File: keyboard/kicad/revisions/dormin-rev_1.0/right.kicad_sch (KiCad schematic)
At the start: 70 parts, among them SW1 SW_PUSH-MX_CHOC, SW10 SW_PUSH-MX_CHOC, SW11 SW_PUSH-MX_CHOC, SW12 SW_PUSH-MX_CHOC, SW13 SW_PUSH-MX_CHOC, SW14 SW_PUSH-MX_CHOC, SW15 SW_PUSH-MX_CHOC, SW16 SW_PUSH-MX_CHOC, SW17 SW_PUSH-MX_CHOC, SW19 SW_PUSH-MX_CHOC, SW2 SW_PUSH-MX_CHOC, SW20 SW_PUSH-MX_CHOC, SW21 SW_PUSH-MX_CHOC, SW22 SW_PUSH-MX_CHOC, SW3 SW_PUSH-MX_CHOC, SW4 SW_PUSH-MX_CHOC, SW5 SW_PUSH-MX_CHOC, SW6 SW_PUSH-MX_CHOC, SW7 SW_PUSH-MX_CHOC, SW8 SW_PUSH-MX_CHOC, SW9 SW_PUSH-MX_CHOC, U1 Seeeduino Xiao nRF52840

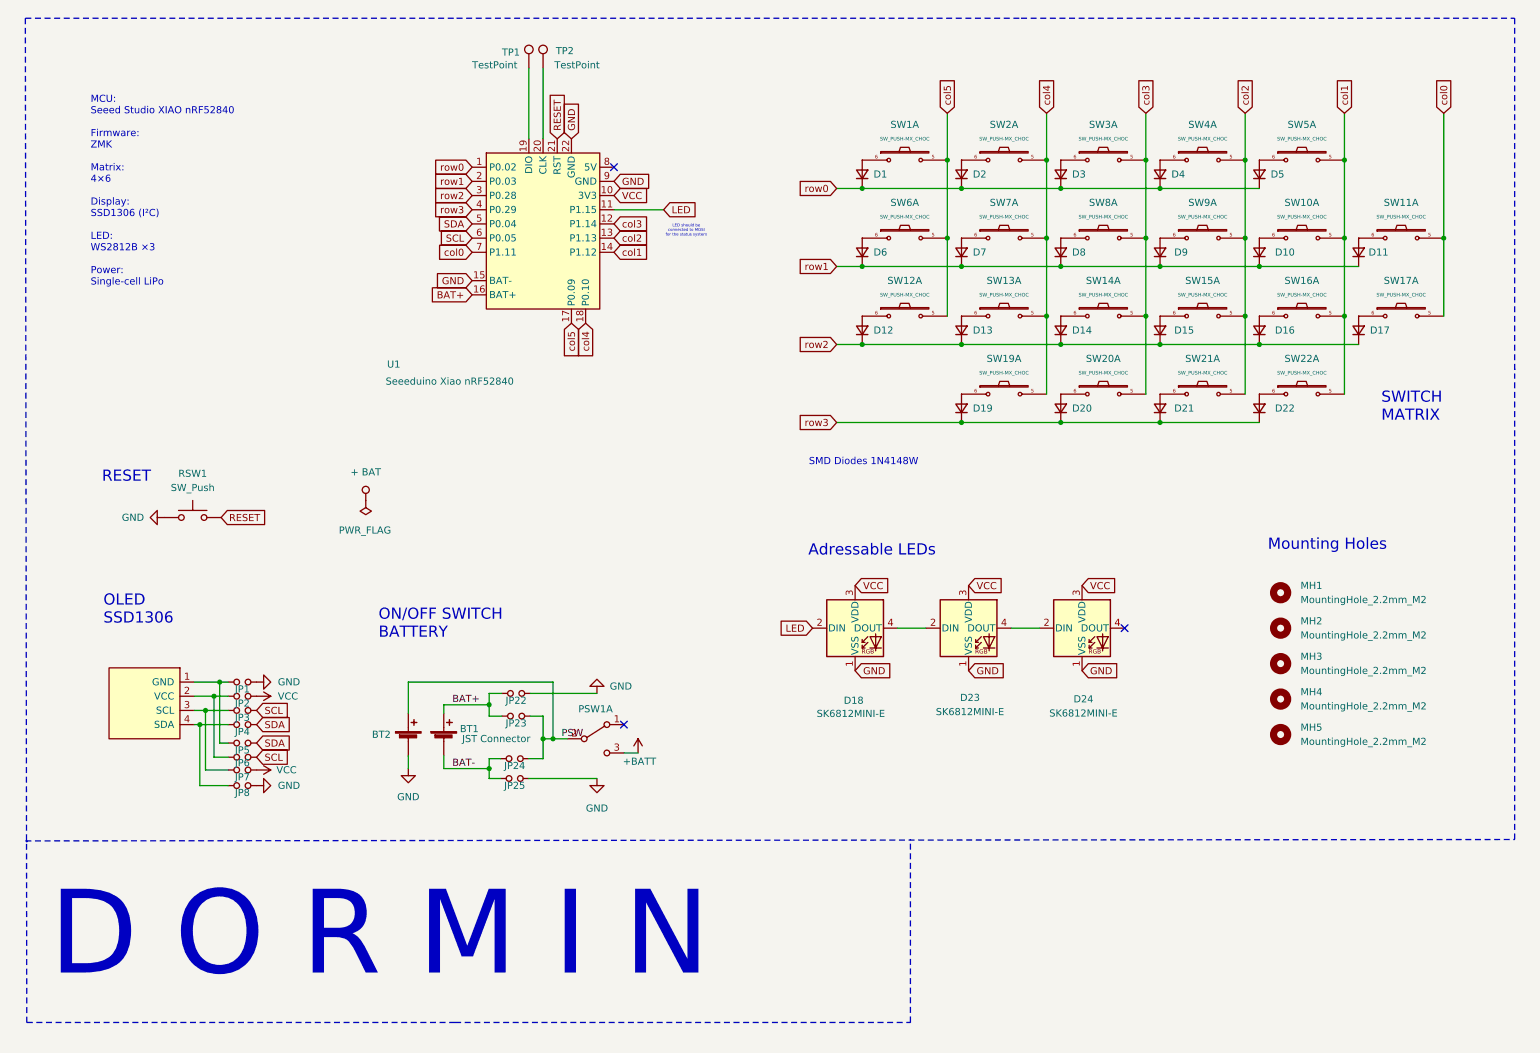
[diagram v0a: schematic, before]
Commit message: feat: update ergogen and kicad
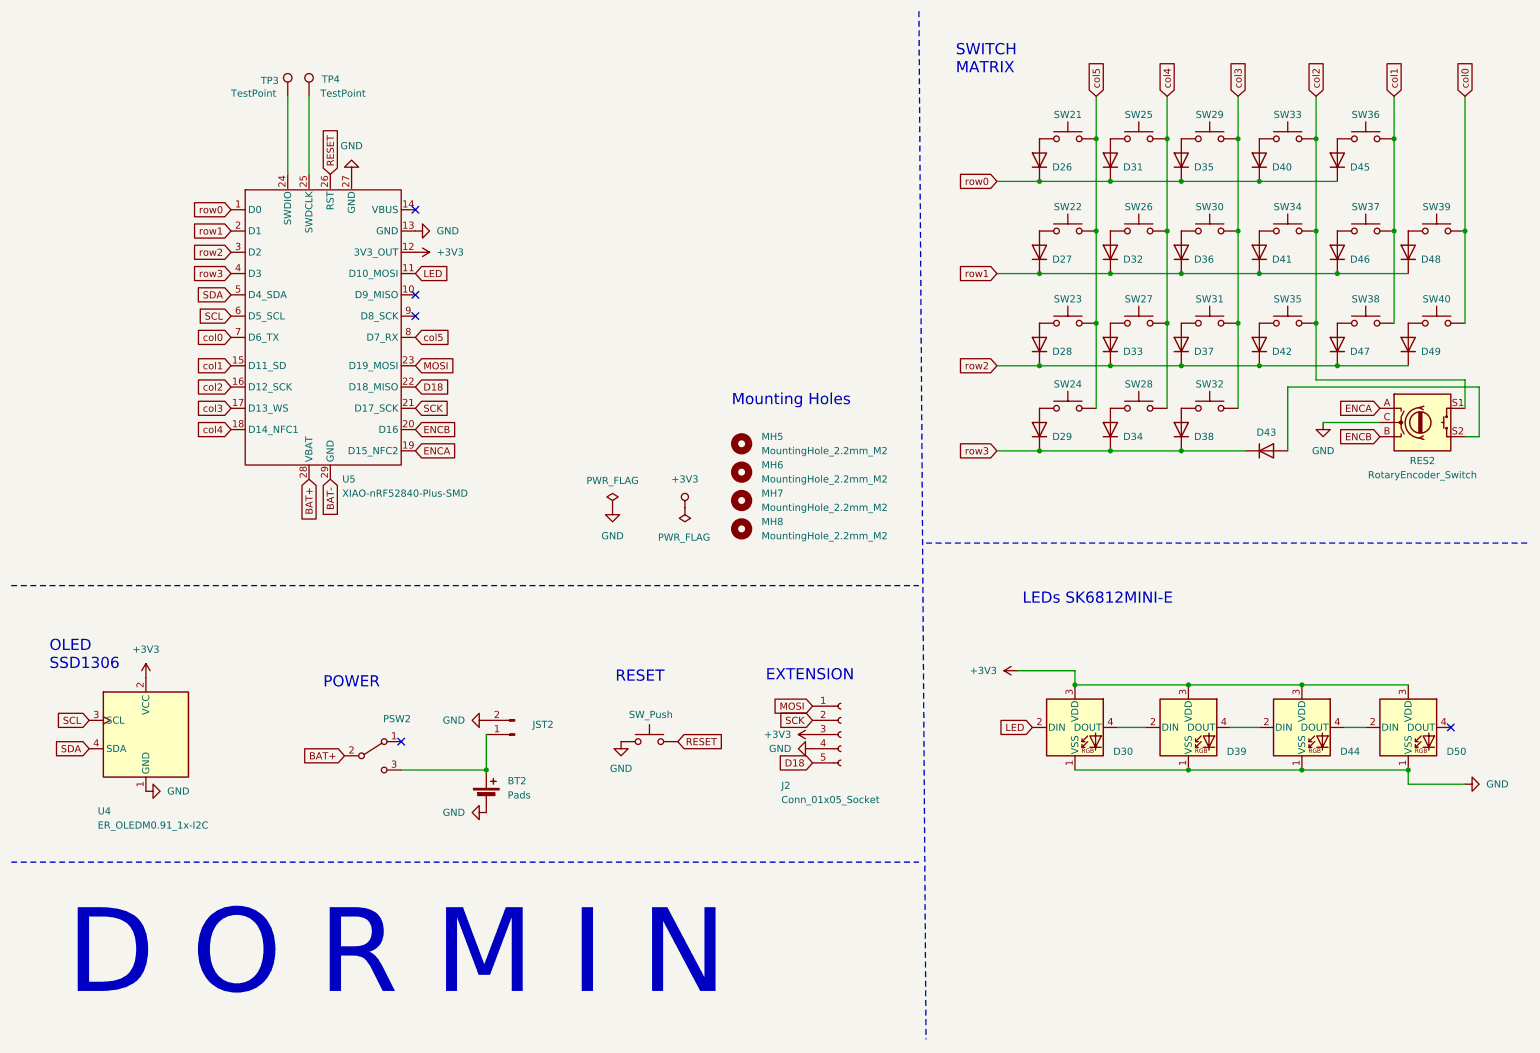
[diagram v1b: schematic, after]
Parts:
- removed BT1: JST Connector, KLOR:JST_PH_reversible, symbol Device:Battery_Cell
- removed D1, D10, D11, D12, D13, D14, D15, D16, D17, D19, D2, D20, D21, D22, D3, D4, D5, D6, D7, D8, D9: D_Small, KLOR:Diode_SOD123, symbol Device:D_Small
- removed D18, D23, D24: SK6812MINI-E, LED_SMD:LED_SK6812MINI-E_3.2x2.8mm_P1.5mm_ReverseMount, symbol LED:SK6812MINI-E
- removed JP1, JP2, JP22, JP23, JP24, JP25, JP3, JP4, JP5, JP6, JP7, JP8: Device_Jumper_NO_Small, KLOR:Jumper, symbol KLORlib:Device_Jumper_NO_Small
- removed MH1, MH2, MH3, MH4: MountingHole_2.2mm_M2, MountingHole:MountingHole_2.2mm_M2, symbol Mechanical:MountingHole
- removed OLED1: SSD1306, ScottoKeebs_Components:OLED_128x32, symbol SSD1306-128x64_OLED:SSD1306
- removed PSW1: SW_DPDT_x2, KLOR:MSK12C02_reversible, symbol Switch:SW_DPDT_x2
- removed RSW1: SW_Push, KLOR:SW_Push_1P1T-MP_NO_Horizontal_Alps_SKRTLAE010_both_sides, symbol Switch:SW_Push
- removed SW1, SW10, SW11, SW12, SW13, SW14, SW15, SW16, SW17, SW19, SW2, SW20, SW21, SW22, SW3, SW4, SW5, SW6, SW7, SW8, SW9: SW_PUSH-MX_CHOC, WillKeebs_Kicad_Gateron:SW_MXchoc_HS_1u, symbol KLORlib:SW_PUSH-MX_W_LED
- removed TP1, TP2: TestPoint, symbol Connector:TestPoint
- removed U1: Seeeduino Xiao nRF52840, PCM_marbastlib-xp-promicroish:Xiao_nRF52840_ACH, symbol PCM_marbastlib-promicroish:Seeeduino_Xiao_nRF52840
- added D26, D27, D28, D29, D31, D32, D33, D34, D35, D36, D37, D38, D40, D41, D42, D43, D45, D46, D47, D48, D49: 1N4148W, Diode_SMD:D_SOD-123, symbol Diode:1N4148W
- added D30, D39, D44, D50: SK6812MINI-E, LED_SMD:LED_SK6812MINI-E_3.2x2.8mm_P1.5mm_ReverseMount, symbol LED:SK6812MINI-E
- added J2: Conn_01x05_Socket, symbol Connector:Conn_01x05_Socket
- added JST2: Conn_01x02_Pin, willkeebs_power:JST_1.25mm, symbol Connector:Conn_01x02_Pin
- added MH6, MH7, MH8: MountingHole_2.2mm_M2, MountingHole:MountingHole_2.2mm_M2, symbol Mechanical:MountingHole
- added PSW2: SW_SPDT, willkeebs_power:Switch_MSK12C02, symbol Switch:SW_SPDT
- added RES2: RotaryEncoder_Switch, willkeebs_peripherals:RotaryEncoder_Alps_EC11E-Switch_Vertical_H20mm-keebio_modified, symbol Device:RotaryEncoder_Switch
- added RSW2: SW_Push, willkeebs_components:SW_Push_1P1T_XKB_TS-1187A, symbol Switch:SW_Push
- added SW21, SW22, SW23, SW24, SW25, SW26, SW27, SW28, SW29, SW30, SW31, SW32, SW33, SW34, SW35, SW36, SW37, SW38, SW39, SW40: SW_Push, willkeebs_keyboard:SW_MX_Choc_Hotswap, symbol Switch:SW_Push
- added TP3, TP4: TestPoint, symbol Connector:TestPoint
- added U4: ER_OLEDM0.91_1x-I2C, Display:ER_OLEDM0.91_1x-I2C, symbol Display_Graphic:ER_OLEDM0.91_1x-I2C
- added U5: XIAO-nRF52840-Plus-SMD, Seeed_Studio_XIAO_Series:XIAO-nRF52840-Plus-SMD, symbol Seeed_Studio_XIAO_Series:XIAO-nRF52840_Plus_SMD
- BT2: value Battery_Cell -> Pads; footprint KLOR:custombatteryconnector_small -> willkeebs_power:Battery_Pad
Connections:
- net BAT+: now also PSW2.2 (B), U5.28 (VBAT)
- net BAT-: now also U5.29 (GND)
- net GND: now also D30.1 (VSS), D39.1 (VSS), D44.1 (VSS), D50.1 (VSS), J2.4 (Pin_4), JST2.2 (Pin_2), RES2.C, RSW2.1, U4.1 (GND), U5.13 (GND), U5.27 (GND)
- net LED: now also D30.2 (DIN), U5.11 (D10_MOSI)
- net RESET: now also RSW2.2, U5.26 (RST)
- net SCL: now also U4.3 (SCL), U5.6 (D5_SCL)
- net SDA: now also U4.4 (SDA), U5.5 (D4_SDA)
- net col0: now also SW39.2, SW40.2, U5.7 (D6_TX)
- net col1: now also SW36.2, SW37.2, SW38.2, U5.15 (D11_SD)
- net col2: now also RES2.S1, SW33.2, SW34.2, SW35.2, U5.16 (D12_SCK)
- net col3: now also SW29.2, SW30.2, SW31.2, SW32.2, U5.17 (D13_WS)
- net col4: now also SW25.2, SW26.2, SW27.2, SW28.2, U5.18 (D14_NFC1)
- net col5: now also SW21.2, SW22.2, SW23.2, SW24.2, U5.8 (D7_RX)
- net row0: now also D26.1 (K), D31.1 (K), D35.1 (K), D40.1 (K), D45.1 (K), U5.1 (D0)
- net row1: now also D27.1 (K), D32.1 (K), D36.1 (K), D41.1 (K), D46.1 (K), D48.1 (K), U5.2 (D1)
- net row2: now also D28.1 (K), D33.1 (K), D37.1 (K), D42.1 (K), D47.1 (K), D49.1 (K), U5.3 (D2)
- net row3: now also D29.1 (K), D34.1 (K), D38.1 (K), D43.1 (K), U5.4 (D3)
- net PSW: no longer names the net of BT2.1 (+)
- net PSW: now also JST2.1 (Pin_1), PSW2.3 (C)
- new net: D26.2 (A), SW21.1
- new net: D36.2 (A), SW30.1
- new net: D49.2 (A), SW40.1
- new net: D43.2 (A), RES2.S2
- new net: D48.2 (A), SW39.1
- new net: D29.2 (A), SW24.1
- new net: D44.4 (DOUT), D50.2 (DIN)
- new net: D35.2 (A), SW29.1
- new net: D28.2 (A), SW23.1
- new net: D45.2 (A), SW36.1
- new net: D40.2 (A), SW33.1
- new net: D34.2 (A), SW28.1
- new net: D47.2 (A), SW38.1
- new net: D42.2 (A), SW35.1
- new net: TP3.1, U5.24 (SWDIO)
- new net: TP4.1, U5.25 (SWDCLK)
- new net: D32.2 (A), SW26.1
- new net: D30.4 (DOUT), D39.2 (DIN)
- new net: D31.2 (A), SW25.1
- new net: D38.2 (A), SW32.1
- new net: D33.2 (A), SW27.1
- new net: D39.4 (DOUT), D44.2 (DIN)
- new net: D27.2 (A), SW22.1
- new net: D37.2 (A), SW31.1
- new net: D46.2 (A), SW37.1
- new net: D41.2 (A), SW34.1
- new net +3V3: D30.3 (VDD), D39.3 (VDD), D44.3 (VDD), D50.3 (VDD), J2.3 (Pin_3), U4.2 (VCC), U5.12 (3V3_OUT)
- new net D18: J2.5 (Pin_5), U5.22 (D18_MISO)
- new net ENCA: RES2.A, U5.19 (D15_NFC2)
- new net ENCB: RES2.B, U5.20 (D16)
- new net MOSI: J2.1 (Pin_1), U5.23 (D19_MOSI)
- new net SCK: J2.2 (Pin_2), U5.21 (D17_SCK)
- no-connect marks 3 -> 5
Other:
- note added: "EXTENSION"
- note added: "LEDs SK6812MINI-E"
- note added: "POWER"
- note removed: "Adressable LEDs"
- note removed: "LED should be connected to MOSI for the status system"
- note removed: "MCU: Seeed Studio XIAO nRF52840 Firmware: ZMK Matrix: 4×6 Display: SSD1306 (I²C) LED: WS2812B ×3 Power: Single-cell LiPo"
- note removed: "ON/OFF SWITCH BATTERY"
- note removed: "SMD Diodes 1N4148W"
- title: Dormin Split Keyboard -> (none)
